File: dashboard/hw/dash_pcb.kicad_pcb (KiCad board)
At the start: 2 copper layers, 0 parts

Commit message: set up lcd shape as the pcb
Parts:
- added J1: LCD, Socket_Strips:Socket_Strip_Straight_2x11_Pitch2.54mm, F.Cu at (261.0, 68.0)
- added J2: DEBUG, Pin_Headers:Pin_Header_Straight_2x05_Pitch1.27mm, F.Cu at (148.5, 105.0)
- added U1: LPC11C24FBD48, Housings_QFP:LQFP-48_7x7mm_Pitch0.5mm, F.Cu at (204.7, 81.8)
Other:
- board outline added: 180 x 65 mm

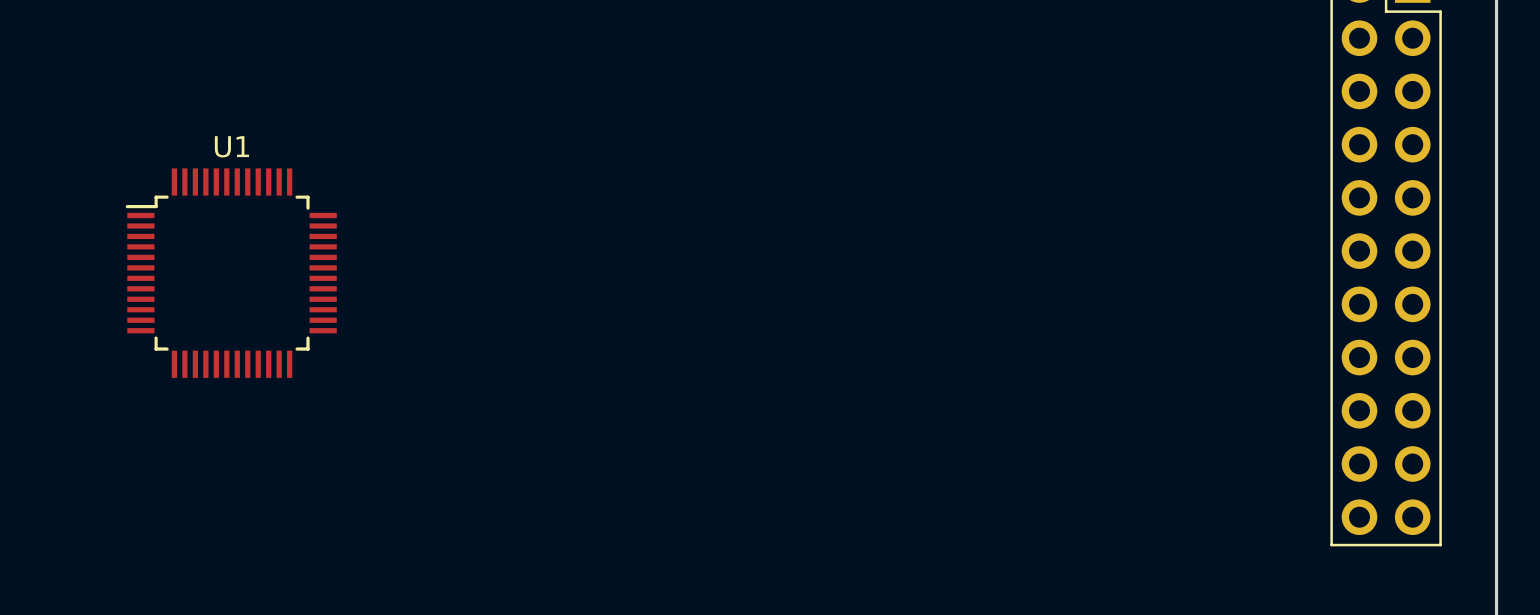
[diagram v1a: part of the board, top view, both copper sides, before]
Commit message: work on laying out LCD connector
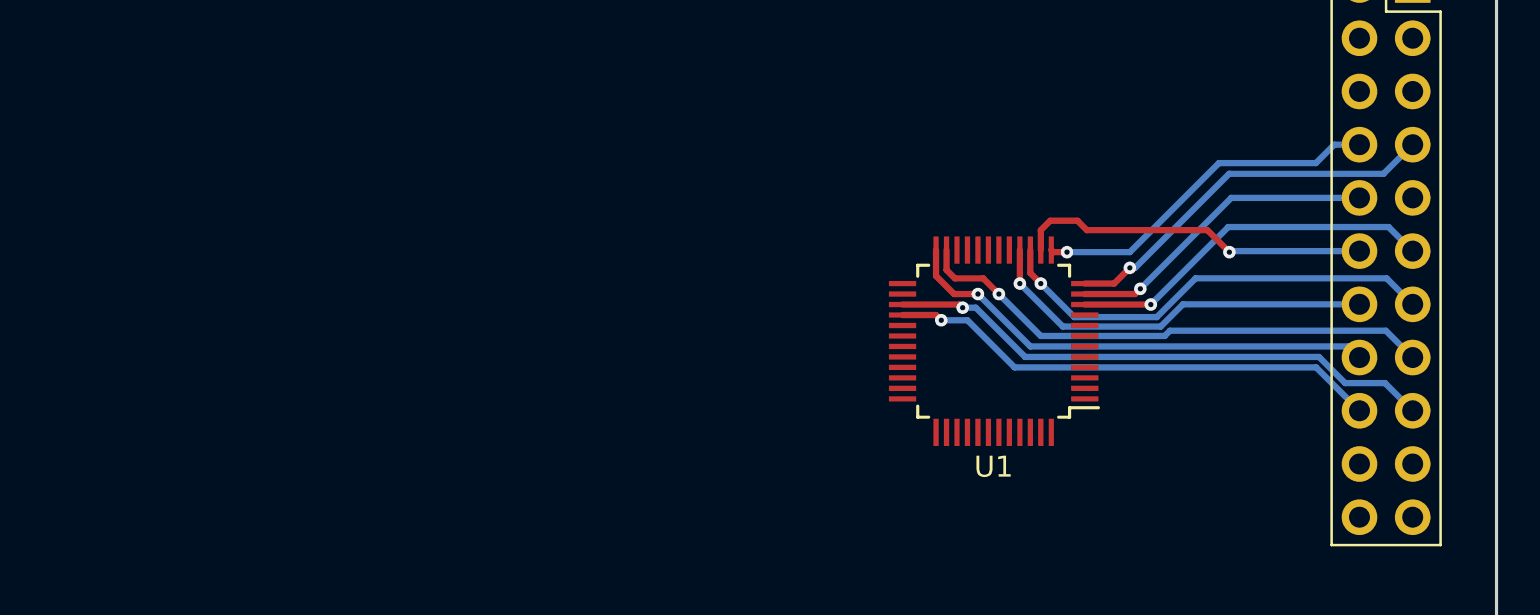
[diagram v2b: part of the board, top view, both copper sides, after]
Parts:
- moved U1 36.5 mm to (241.0, 85.0), turned to 180 degrees
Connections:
- U1 pad 11: Net-(U1-Pad11) -> /LCD_~RST
- U1 pad 12: Net-(U1-Pad12) -> /LCD_~CE
- U1 pad 13: Net-(U1-Pad13) -> /LCD_D/~C
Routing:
- net /LCD_DB6: track 0.00 -> 26.5 mm, vias 0 -> 1
- net /LCD_DB4: track 0.00 -> 25.1 mm, vias 0 -> 1
- net /LCD_DB7: track 0.00 -> 23.7 mm, vias 0 -> 1
- net /LCD_DB5: track 0.00 -> 23.1 mm, vias 0 -> 1
- net /LCD_DB2: track 0.00 -> 21.5 mm, vias 0 -> 1
- net /LCD_DB3: track 0.00 -> 19.1 mm, vias 0 -> 1
- net /LCD_~CE: track 0.00 -> 18.4 mm, vias 0 -> 1
- net /LCD_DB0: track 0.00 -> 17.7 mm, vias 0 -> 1
- net /LCD_DB1: track 0.00 -> 17.0 mm, vias 0 -> 1
- net /LCD_D/~C: track 0.00 -> 16.9 mm, vias 0 -> 1
- net /LCD_~RST: track 0.00 -> 15.0 mm, vias 0 -> 1

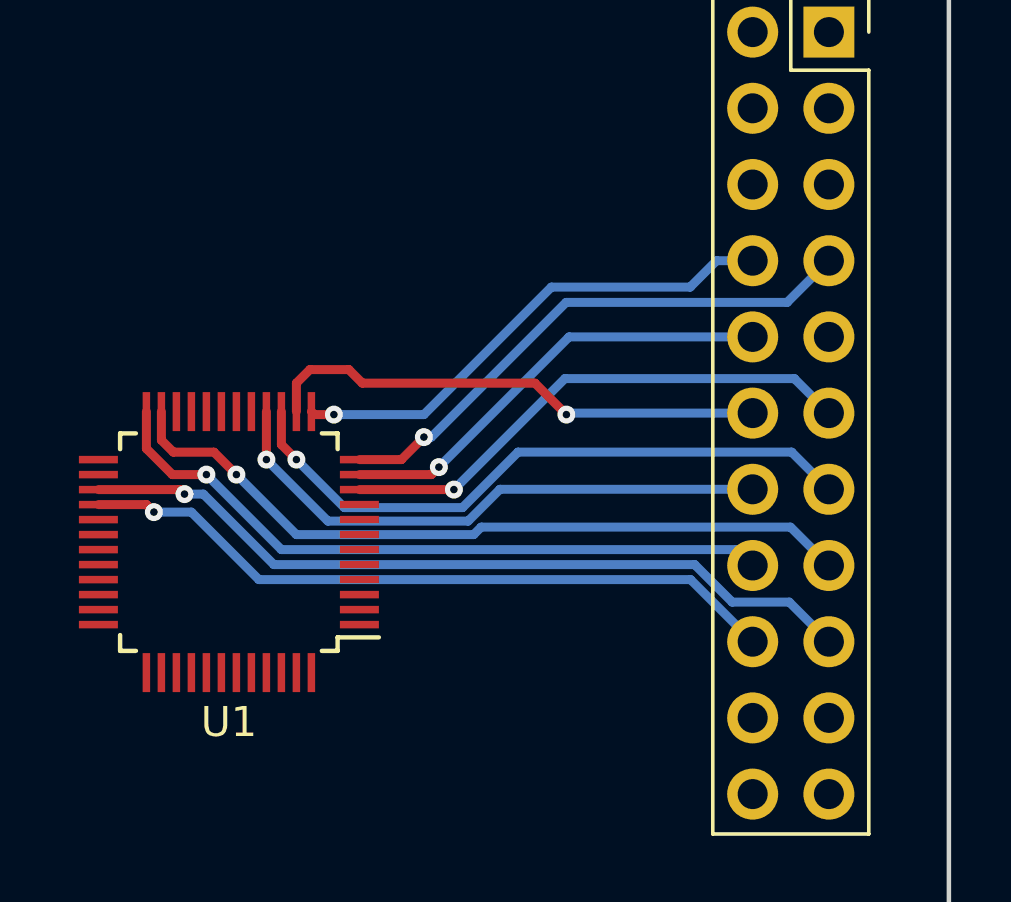
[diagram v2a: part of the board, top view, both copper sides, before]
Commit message: finish prototype lcd wire
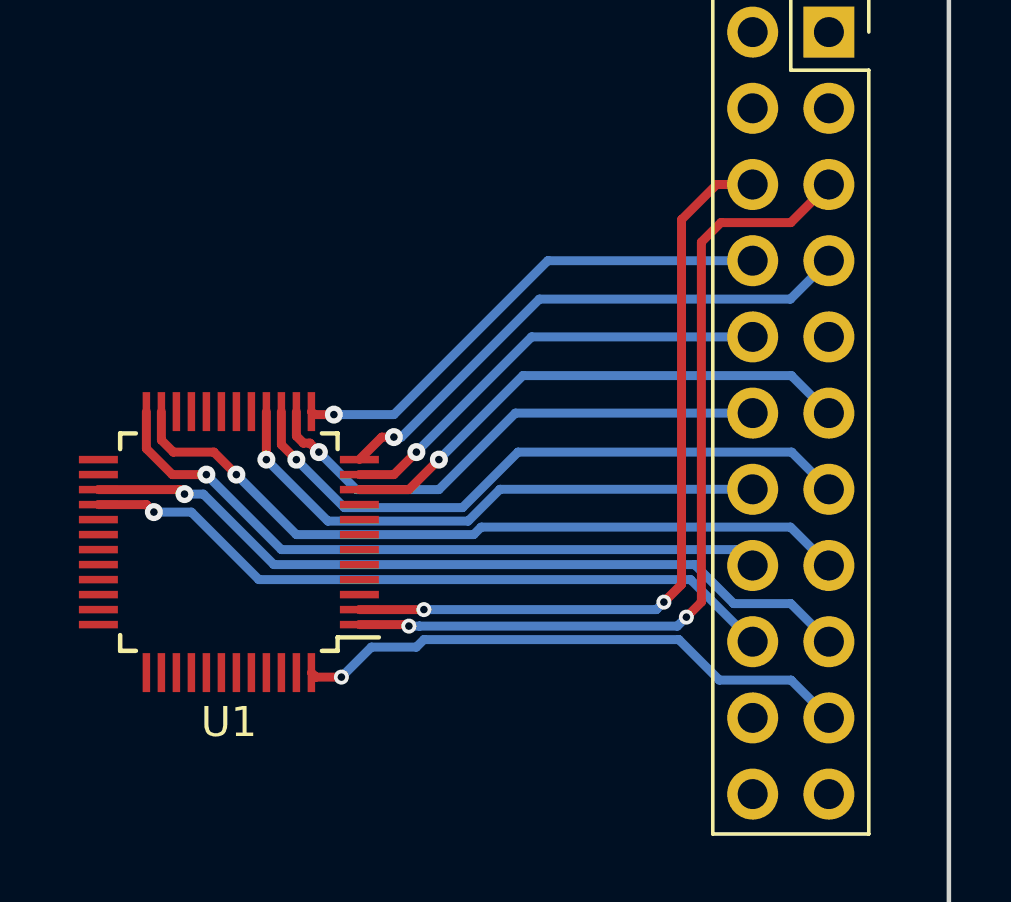
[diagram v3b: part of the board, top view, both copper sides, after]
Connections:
- U1 pad 1: Net-(U1-Pad1) -> /LCD_~WR
- U1 pad 2: Net-(U1-Pad2) -> /LCD_~RD
- U1 pad 48: Net-(U1-Pad48) -> /LCD_FS
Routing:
- net /LCD_~WR: track 0.00 -> 29.6 mm, vias 0 -> 2
- net /LCD_~RD: track 0.00 -> 26.1 mm, vias 0 -> 2
- net /LCD_FS: track 0.00 -> 18.9 mm, vias 0 -> 1
- net /LCD_DB1: track 17.0 -> 17.8 mm

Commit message: label a couple more required pins
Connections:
- net Net-(U1-Pad18) renamed /CANL
- net Net-(U1-Pad19) renamed /CANH
- net Net-(U1-Pad6) renamed /XTALIN
- net Net-(U1-Pad7) renamed /XTALOUT
- U1 pad 22: Net-(U1-Pad22) -> GND
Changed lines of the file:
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@@
 (kicad_pcb (version 4) (host pcbnew 4.0.7)
   (general
-    (links 29)
-    (no_connects 15)
+    (links 30)
+    (no_connects 16)
     (area 84.924999 54.924999 265.075001 120.075001)
     (thickness 1.6)
@@
     (zones 0)
     (modules 3)
-    (nets 52)
+    (nets 51)
   )
   (page A4)
@@
   )
   (setup
-    (last_trace_width 0.3)
+    (last_trace_width 0.15)
     (user_trace_width 0.2)
     (user_trace_width 0.3)
@@
   (net 27 "Net-(J2-Pad8)")
   (net 28 /MCU_~RESET)
-  (net 29 "Net-(U1-Pad6)")
-  (net 30 "Net-(U1-Pad7)")
-  (net 31 "Net-(U1-Pad9)")
-  (net 32 "Net-(U1-Pad18)")
-  (net 33 "Net-(U1-Pad19)")
-  (net 34 "Net-(U1-Pad22)")
-  (net 35 "Net-(U1-Pad25)")
-  (net 36 "Net-(U1-Pad26)")
-  (net 37 "Net-(U1-Pad30)")
-  (net 38 "Net-(U1-Pad31)")
-  (net 39 "Net-(U1-Pad32)")
-  (net 40 "Net-(U1-Pad33)")
-  (net 41 "Net-(U1-Pad34)")
-  (net 42 "Net-(U1-Pad35)")
-  (net 43 "Net-(U1-Pad36)")
-  (net 44 "Net-(U1-Pad37)")
-  (net 45 "Net-(U1-Pad38)")
-  (net 46 "Net-(U1-Pad40)")
-  (net 47 "Net-(U1-Pad42)")
-  (net 48 "Net-(U1-Pad43)")
-  (net 49 "Net-(U1-Pad45)")
-  (net 50 "Net-(U1-Pad46)")
-  (net 51 "Net-(U1-Pad47)")
+  (net 29 "Net-(U1-Pad9)")
+  (net 30 "Net-(U1-Pad25)")
+  (net 31 "Net-(U1-Pad26)")
+  (net 32 "Net-(U1-Pad30)")
+  (net 33 "Net-(U1-Pad31)")
+  (net 34 "Net-(U1-Pad32)")
+  (net 35 "Net-(U1-Pad33)")
+  (net 36 "Net-(U1-Pad34)")
+  (net 37 "Net-(U1-Pad35)")
+  (net 38 "Net-(U1-Pad36)")
+  (net 39 "Net-(U1-Pad37)")
+  (net 40 "Net-(U1-Pad38)")
+  (net 41 "Net-(U1-Pad40)")
+  (net 42 "Net-(U1-Pad42)")
+  (net 43 "Net-(U1-Pad43)")
+  (net 44 "Net-(U1-Pad45)")
+  (net 45 "Net-(U1-Pad46)")
+  (net 46 "Net-(U1-Pad47)")
+  (net 47 /XTALIN)
+  (net 48 /XTALOUT)
+  (net 49 /CANL)
+  (net 50 /CANH)
   (net_class Default "This is the default net class."
     (clearance 0.15)
@@
     (add_net +3V3)
     (add_net +5V)
+    (add_net /CANH)
+    (add_net /CANL)
     (add_net /LCD_D/~C)
     (add_net /LCD_DB0)
@@
     (add_net /SWCLK)
     (add_net /SWDIO)
+    (add_net /XTALIN)
+    (add_net /XTALOUT)
     (add_net GND)
     (add_net "Net-(J1-Pad9)")
@@
     (add_net "Net-(J2-Pad7)")
     (add_net "Net-(J2-Pad8)")
-    (add_net "Net-(U1-Pad18)")
-    (add_net "Net-(U1-Pad19)")
-    (add_net "Net-(U1-Pad22)")
     (add_net "Net-(U1-Pad25)")
     (add_net "Net-(U1-Pad26)")
@@
     (add_net "Net-(U1-Pad46)")
     (add_net "Net-(U1-Pad47)")
-    (add_net "Net-(U1-Pad6)")
-    (add_net "Net-(U1-Pad7)")
     (add_net "Net-(U1-Pad9)")
   )
@@
       (net 1 GND))
     (pad 6 smd rect (at -4.35 -0.25 180) (size 1.3 0.25) (layers F.Cu F.Paste F.Mask)
-      (net 29 "Net-(U1-Pad6)"))
+      (net 47 /XTALIN))
     (pad 7 smd rect (at -4.35 0.25 180) (size 1.3 0.25) (layers F.Cu F.Paste F.Mask)
-      (net 30 "Net-(U1-Pad7)"))
+      (net 48 /XTALOUT))
     (pad 8 smd rect (at -4.35 0.75 180) (size 1.3 0.25) (layers F.Cu F.Paste F.Mask)
       (net 22 +3V3))
     (pad 9 smd rect (at -4.35 1.25 180) (size 1.3 0.25) (layers F.Cu F.Paste F.Mask)
-      (net 31 "Net-(U1-Pad9)"))
+      (net 29 "Net-(U1-Pad9)"))
     (pad 10 smd rect (at -4.35 1.75 180) (size 1.3 0.25) (layers F.Cu F.Paste F.Mask)
       (net 10 /LCD_DB0))
@@
       (net 22 +3V3))
     (pad 18 smd rect (at -0.25 4.35 270) (size 1.3 0.25) (layers F.Cu F.Paste F.Mask)
-      (net 32 "Net-(U1-Pad18)"))
+      (net 49 /CANL))
     (pad 19 smd rect (at 0.25 4.35 270) (size 1.3 0.25) (layers F.Cu F.Paste F.Mask)
-      (net 33 "Net-(U1-Pad19)"))
+      (net 50 /CANH))
     (pad 20 smd rect (at 0.75 4.35 270) (size 1.3 0.25) (layers F.Cu F.Paste F.Mask)
       (net 2 +5V))
@@
       (net 1 GND))
     (pad 22 smd rect (at 1.75 4.35 270) (size 1.3 0.25) (layers F.Cu F.Paste F.Mask)
-      (net 34 "Net-(U1-Pad22)"))
+      (net 1 GND))
     (pad 23 smd rect (at 2.25 4.35 270) (size 1.3 0.25) (layers F.Cu F.Paste F.Mask)
       (net 14 /LCD_DB4))
@@
       (net 15 /LCD_DB5))
     (pad 25 smd rect (at 4.35 2.75 180) (size 1.3 0.25) (layers F.Cu F.Paste F.Mask)
-      (net 35 "Net-(U1-Pad25)"))
+      (net 30 "Net-(U1-Pad25)"))
     (pad 26 smd rect (at 4.35 2.25 180) (size 1.3 0.25) (layers F.Cu F.Paste F.Mask)
-      (net 36 "Net-(U1-Pad26)"))
+      (net 31 "Net-(U1-Pad26)"))
     (pad 27 smd rect (at 4.35 1.75 180) (size 1.3 0.25) (layers F.Cu F.Paste F.Mask)
       (net 16 /LCD_DB6))
@@
       (net 24 /SWCLK))
     (pad 30 smd rect (at 4.35 0.25 180) (size 1.3 0.25) (layers F.Cu F.Paste F.Mask)
-      (net 37 "Net-(U1-Pad30)"))
+      (net 32 "Net-(U1-Pad30)"))
     (pad 31 smd rect (at 4.35 -0.25 180) (size 1.3 0.25) (layers F.Cu F.Paste F.Mask)
-      (net 38 "Net-(U1-Pad31)"))
+      (net 33 "Net-(U1-Pad31)"))
     (pad 32 smd rect (at 4.35 -0.75 180) (size 1.3 0.25) (layers F.Cu F.Paste F.Mask)
-      (net 39 "Net-(U1-Pad32)"))
+      (net 34 "Net-(U1-Pad32)"))
     (pad 33 smd rect (at 4.35 -1.25 180) (size 1.3 0.25) (layers F.Cu F.Paste F.Mask)
-      (net 40 "Net-(U1-Pad33)"))
+      (net 35 "Net-(U1-Pad33)"))
     (pad 34 smd rect (at 4.35 -1.75 180) (size 1.3 0.25) (layers F.Cu F.Paste F.Mask)
-      (net 41 "Net-(U1-Pad34)"))
+      (net 36 "Net-(U1-Pad34)"))
     (pad 35 smd rect (at 4.35 -2.25 180) (size 1.3 0.25) (layers F.Cu F.Paste F.Mask)
-      (net 42 "Net-(U1-Pad35)"))
+      (net 37 "Net-(U1-Pad35)"))
     (pad 36 smd rect (at 4.35 -2.75 180) (size 1.3 0.25) (layers F.Cu F.Paste F.Mask)
-      (net 43 "Net-(U1-Pad36)"))
+      (net 38 "Net-(U1-Pad36)"))
     (pad 37 smd rect (at 2.75 -4.35 270) (size 1.3 0.25) (layers F.Cu F.Paste F.Mask)
-      (net 44 "Net-(U1-Pad37)"))
+      (net 39 "Net-(U1-Pad37)"))
     (pad 38 smd rect (at 2.25 -4.35 270) (size 1.3 0.25) (layers F.Cu F.Paste F.Mask)
-      (net 45 "Net-(U1-Pad38)"))
+      (net 40 "Net-(U1-Pad38)"))
     (pad 39 smd rect (at 1.75 -4.35 270) (size 1.3 0.25) (layers F.Cu F.Paste F.Mask)
       (net 23 /SWDIO))
     (pad 40 smd rect (at 1.25 -4.35 270) (size 1.3 0.25) (layers F.Cu F.Paste F.Mask)
-      (net 46 "Net-(U1-Pad40)"))
+      (net 41 "Net-(U1-Pad40)"))
     (pad 41 smd rect (at 0.75 -4.35 270) (size 1.3 0.25) (layers F.Cu F.Paste F.Mask)
       (net 1 GND))
     (pad 42 smd rect (at 0.25 -4.35 270) (size 1.3 0.25) (layers F.Cu F.Paste F.Mask)
-      (net 47 "Net-(U1-Pad42)"))
+      (net 42 "Net-(U1-Pad42)"))
     (pad 43 smd rect (at -0.25 -4.35 270) (size 1.3 0.25) (layers F.Cu F.Paste F.Mask)
-      (net 48 "Net-(U1-Pad43)"))
+      (net 43 "Net-(U1-Pad43)"))
     (pad 44 smd rect (at -0.75 -4.35 270) (size 1.3 0.25) (layers F.Cu F.Paste F.Mask)
       (net 22 +3V3))
     (pad 45 smd rect (at -1.25 -4.35 270) (size 1.3 0.25) (layers F.Cu F.Paste F.Mask)
-      (net 49 "Net-(U1-Pad45)"))
+      (net 44 "Net-(U1-Pad45)"))
     (pad 46 smd rect (at -1.75 -4.35 270) (size 1.3 0.25) (layers F.Cu F.Paste F.Mask)
-      (net 50 "Net-(U1-Pad46)"))
+      (net 45 "Net-(U1-Pad46)"))
     (pad 47 smd rect (at -2.25 -4.35 270) (size 1.3 0.25) (layers F.Cu F.Paste F.Mask)
-      (net 51 "Net-(U1-Pad47)"))
+      (net 46 "Net-(U1-Pad47)"))
     (pad 48 smd rect (at -2.75 -4.35 270) (size 1.3 0.25) (layers F.Cu F.Paste F.Mask)
       (net 18 /LCD_FS))

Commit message: misnamed command data pin on lcd
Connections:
- net /LCD_D/~C renamed /LCD_C/~D

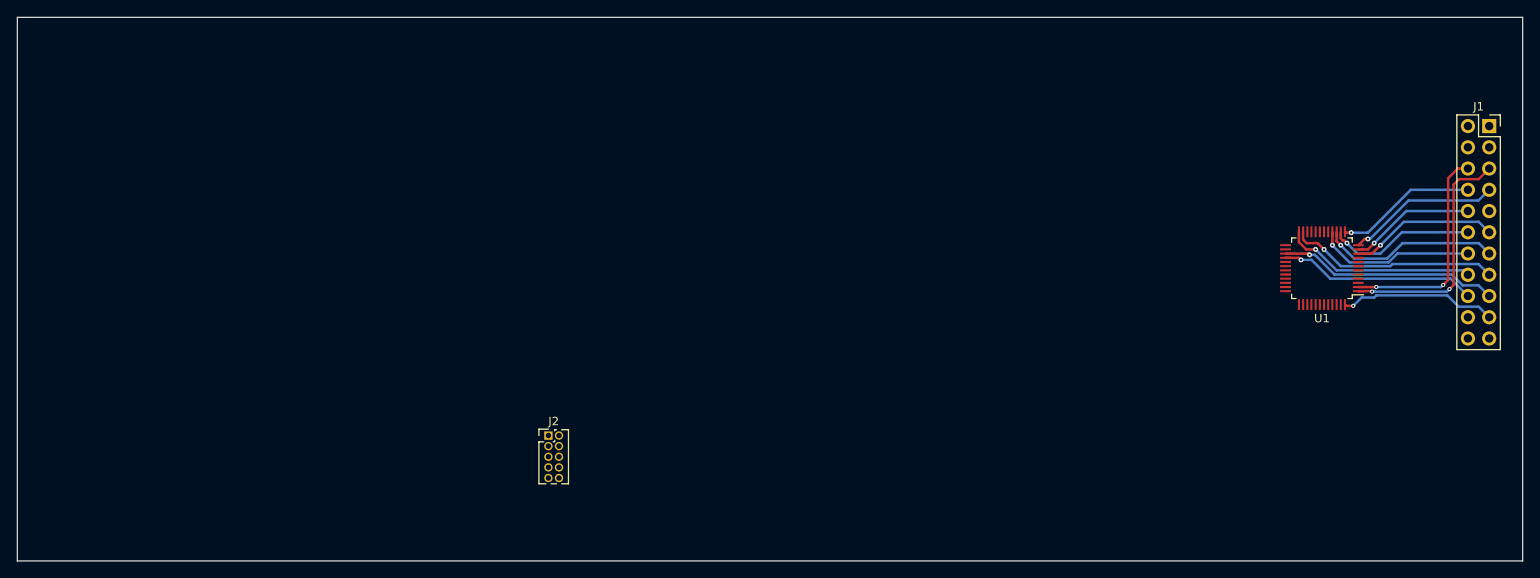
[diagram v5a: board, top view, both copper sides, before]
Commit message: update connectors for the lcd actually used
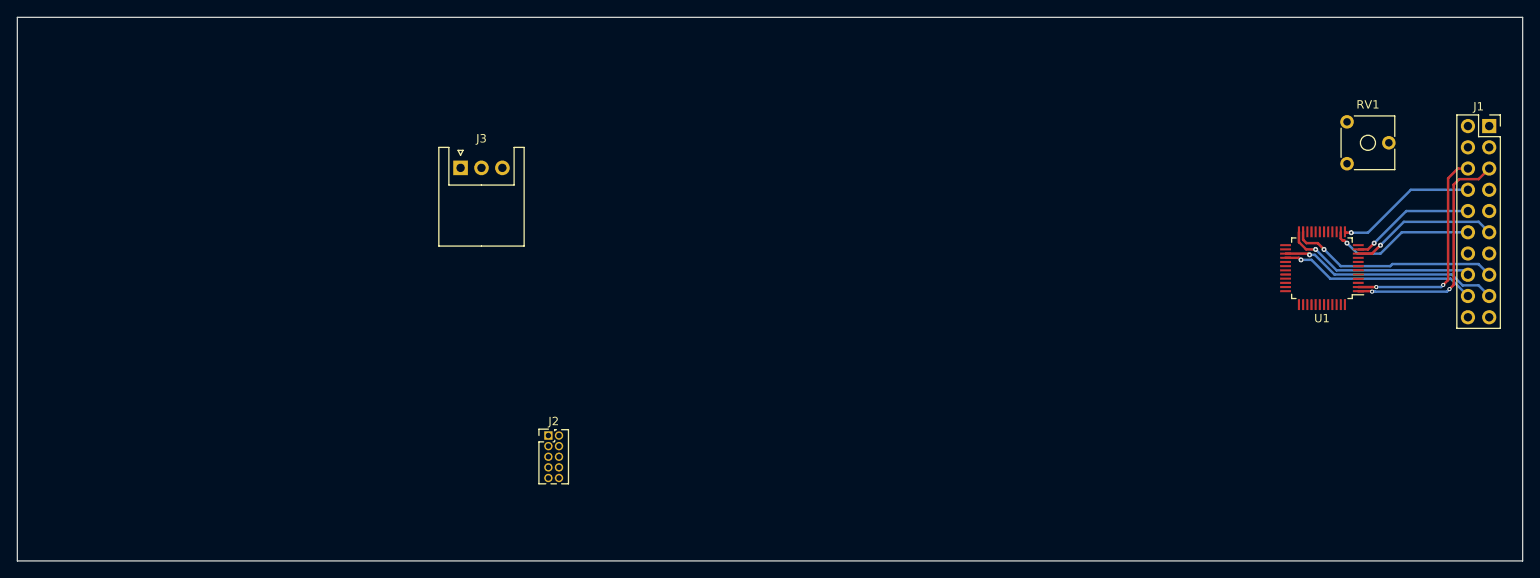
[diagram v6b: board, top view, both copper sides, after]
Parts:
- added J3: LCD_BL, Connectors_JST:JST_XH_S03B-XH-A_03x2.50mm_Angled, F.Cu at (138.0, 73.0)
- added RV1: 10k, Potentiometers:Potentiometer_Trimmer_ACP_CA6v_Horizontal, F.Cu at (244.0, 72.5)
- J1: footprint Socket_Strips:Socket_Strip_Straight_2x11_Pitch2.54mm -> Socket_Strips:Socket_Strip_Straight_2x10_Pitch2.54mm
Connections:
- J1 pad 19: /LCD_FS -> +3V3
- J1 pad 20: /LCD_VEE -> Net-(J1-Pad20)
- J1 pad 3: +5V -> +3V3
- J1 pad 7: /LCD_~CE -> GND
- J1 pad 9: Net-(J1-Pad9) -> /LCD_VEE
- U1 pad 12: /LCD_~CE -> Net-(U1-Pad12)
- U1 pad 15: /LCD_DB2 -> Net-(U1-Pad15)
- U1 pad 16: /LCD_DB3 -> Net-(U1-Pad16)
- U1 pad 45: Net-(U1-Pad45) -> /LCD_DB3
- U1 pad 48: /LCD_FS -> Net-(U1-Pad48)
- U1 pad 9: Net-(U1-Pad9) -> /LCD_DB2
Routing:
- net /LCD_DB2: track 21.5 -> 0.00 mm, vias 1 -> 0
- net /LCD_DB3: track 19.1 -> 0.00 mm, vias 1 -> 0
- net /LCD_FS: track 18.9 -> 0.00 mm, vias 1 -> 0
- net /LCD_~CE: track 18.4 -> 0.00 mm, vias 1 -> 0
